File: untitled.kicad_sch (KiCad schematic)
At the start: 10 parts, among them J3 DSUB-9_Female_Horizontal_P2.7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

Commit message: More schematic tidying
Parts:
- J3: symbol Connector:DE9_Socket_MountingHoles -> apc-custom:APC_smart_RS232_DE9_socket
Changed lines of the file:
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@@
 	)
 	(symbol
-		(lib_id "Connector:DE9_Socket_MountingHoles")
+		(lib_id "apc-custom:APC_smart_RS232_DE9_socket")
 		(at 261.62 66.04 0)
 		(unit 1)
@@
 			)
 		)
-		(property "Description" ""
+		(property "Description" "9-pin D-SUB connector, socket (female), Mounting Hole"
 			(at 261.62 66.04 0)
 			(effects

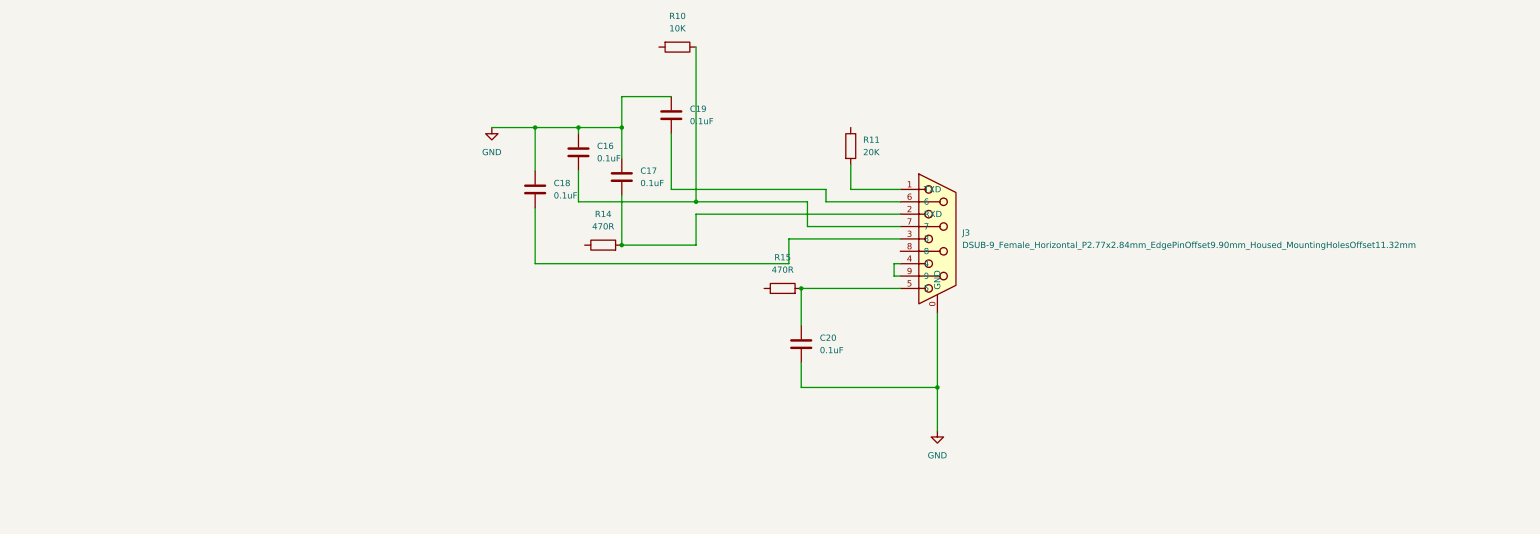
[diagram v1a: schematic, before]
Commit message: Add placeholder components for unknown ICs
Finish the serial interface schematic
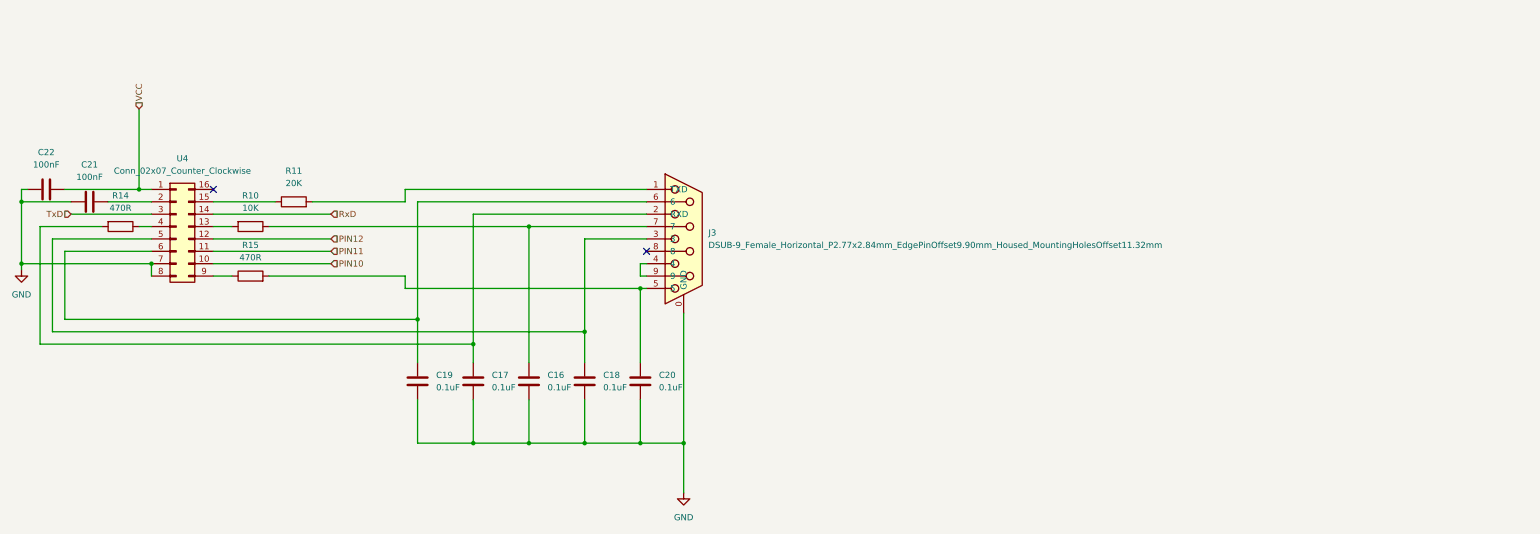
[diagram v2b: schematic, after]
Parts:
- added C21, C22: 100nF, apc-custom:C_Tant_L9.0mm_W2.5mm_P7.50mm_MKT, symbol Device:C
- added U4: Conn_02x07_Counter_Clockwise, Package_DIP:DIP-16_W7.62mm, symbol Connector_Generic:Conn_02x08_Counter_Clockwise
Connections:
- net GND: now also C21.1, C22.1, U4.7 (Pin_7), U4.8 (Pin_8)
- net at R10.2: now also U4.13 (Pin_13)
- net at C18.2, J3.3: now also U4.5 (Pin_5)
- net at C19.2, J3.6: now also U4.6 (Pin_6)
- net at R14.1: now also U4.4 (Pin_4)
- net at R15.1: now also U4.9 (Pin_9)
- net at R11.1: now also U4.15 (Pin_15)
- new net: C21.2, U4.2 (Pin_2)
- new net PIN10: U4.10 (Pin_10)
- new net PIN11: U4.11 (Pin_11)
- new net PIN12: U4.12 (Pin_12)
- new net RxD: U4.14 (Pin_14)
- new net TxD: U4.3 (Pin_3)
- new net VCC: C22.2, U4.1 (Pin_1)
- no-connect marks 0 -> 2
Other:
- moved on the sheet: C16, C17, C18, C19, C20, J3, R10, R11, R14, R15
